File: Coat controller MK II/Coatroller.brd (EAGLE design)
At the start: 100 x 80 mm, 3 parts, among them U1 ATMEGA328P_PDIP, U2 V_REG_LDOSMD, Y1 ABM3B-16.000MHZ-B2-T

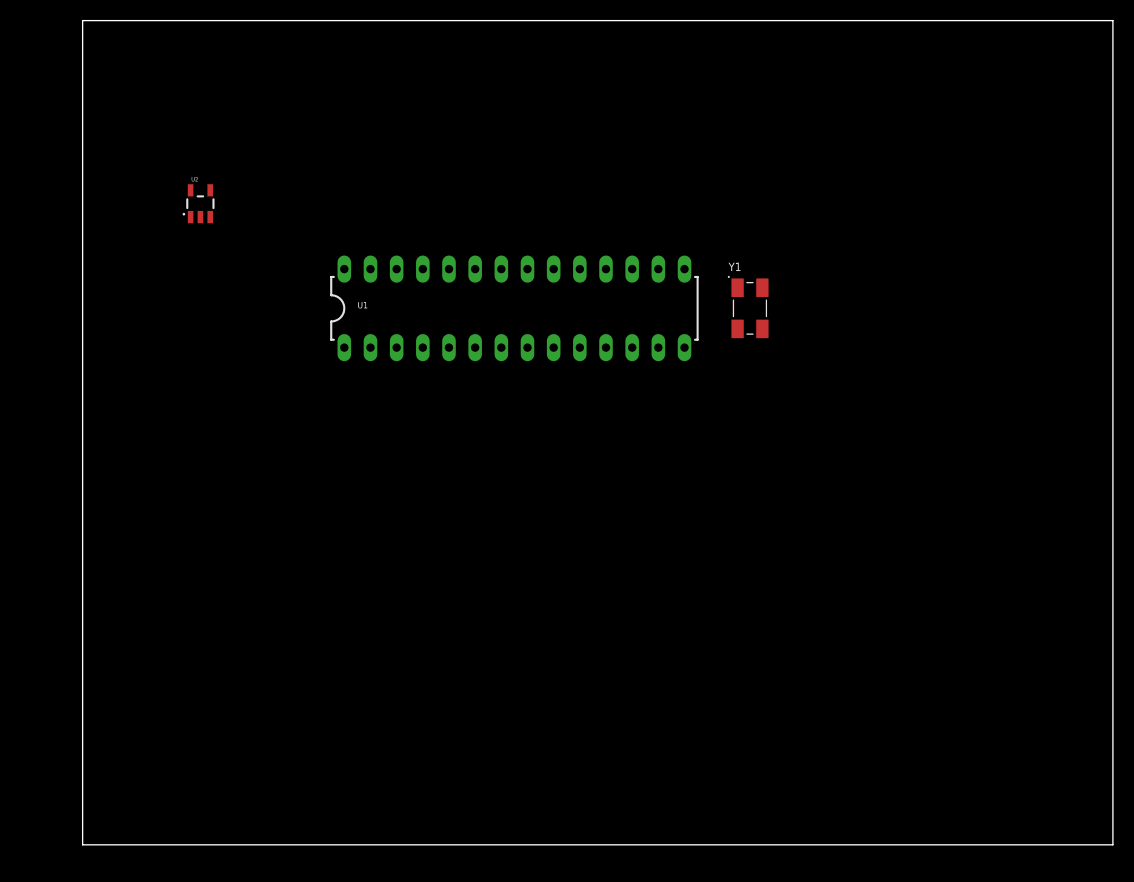
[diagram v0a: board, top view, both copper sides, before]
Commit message: added more parts
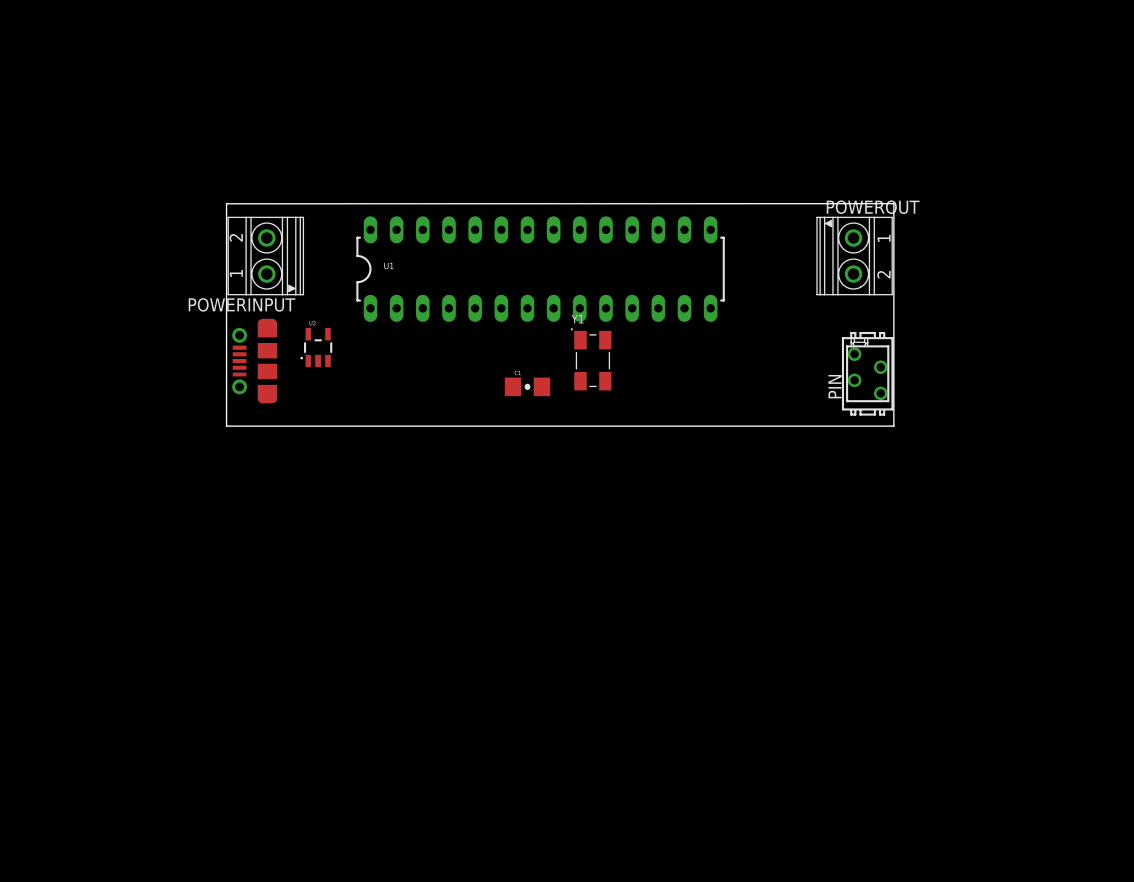
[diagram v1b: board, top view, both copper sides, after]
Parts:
- added C1: (no value), SparkFun-Capacitors:1206-CAP
- added PIN: MICROMATCH-4, con-amp-micromatch:MICROMATCH-4
- added POWERINPUT, POWEROUT: 1751248, con-phoenix-350:1751248
- added U$1: USB-CON-5PIN-105017-0001, GeekAmmo:USB-MICRO-MOLEX-105017-0001
- moved U2 18.1 mm to (22.9, 48.3)
- moved Y1 16.1 mm to (49.5, 47.0)
- moved U1 4.58 mm to (44.5, 55.9)
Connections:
- new net 5V: U1.7, U2.5
- new net GROUND: C1.2, PIN.4, POWERINPUT.1, POWEROUT.2, U$1.5, U1.8, U2.2
- new net N$1: U1.9, Y1.1
- new net N$2: U1.10, Y1.3
- new net N$3: C1.1, Y1.2, Y1.4
- new net N$4: PIN.3, U1.13
- new net N$5: PIN.2, U1.4
- new net VCC: PIN.1, POWERINPUT.2, POWEROUT.1, U$1.1, U2.1, U2.3
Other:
- board size 100 x 80 mm -> 64.8 x 21.6 mm
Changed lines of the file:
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@@
 <board>
 <plain>
-<wire x1="0" y1="0" x2="100" y2="0" width="0" layer="20"/>
-<wire x1="100" y1="0" x2="100" y2="80" width="0" layer="20"/>
-<wire x1="100" y1="80" x2="0" y2="80" width="0" layer="20"/>
-<wire x1="0" y1="80" x2="0" y2="0" width="0" layer="20"/>
+<wire x1="13.97" y1="40.64" x2="78.74" y2="40.64" width="0" layer="20"/>
+<wire x1="78.74" y1="40.64" x2="78.74" y2="62.23" width="0" layer="20"/>
+<wire x1="78.74" y1="62.23" x2="13.97" y2="62.22" width="0" layer="20"/>
+<wire x1="13.97" y1="62.22" x2="13.97" y2="40.64" width="0" layer="20"/>
 </plain>
 <attributes>
@@
 </autorouter>
 <elements>
-<element name="U1" library="SparkFun-DigitalIC" package="DIL28-3" value="ATMEGA328P_PDIP" x="41.91" y="52.07"/>
-<element name="U2" library="SparkFun-PowerIC" package="SOT23-5" value="V_REG_LDOSMD" x="11.43" y="62.23"/>
-<element name="Y1" library="ABM3B-16.000MHZ-B2-T" package="OSCSC500X320X110-4N" value="ABM3B-16.000MHZ-B2-T" x="64.77" y="52.07">
-<attribute name="PRICE" value="0.52 USD" x="64.77" y="52.07" size="1.778" layer="27" display="off"/>
-<attribute name="MP" value="ABM3B-16.000MHZ-B2-T" x="64.77" y="52.07" size="1.778" layer="27" display="off"/>
-<attribute name="PACKAGE" value="5.0 x 3.2mm Abracon" x="64.77" y="52.07" size="1.778" layer="27" display="off"/>
-<attribute name="DESCRIPTION" value="Crystal 16MHz %3F%3F20ppm %28Tol%29 %3F%3F50ppm %28Stability%29 18pF FUND 50Ohm 4-Pin CSMD T/R" x="64.77" y="52.07" size="1.778" layer="27" display="off"/>
-<attribute name="MF" value="Abracon" x="64.77" y="52.07" size="1.778" layer="27" display="off"/>
-<attribute name="AVAILABILITY" value="Good" x="64.77" y="52.07" size="1.778" layer="27" display="off"/>
+<element name="U1" library="SparkFun-DigitalIC" package="DIL28-3" value="ATMEGA328P_PDIP" x="44.45" y="55.88"/>
+<element name="U2" library="SparkFun-PowerIC" package="SOT23-5" value="V_REG_LDOSMD" x="22.86" y="48.26"/>
+<element name="Y1" library="ABM3B-16.000MHZ-B2-T" package="OSCSC500X320X110-4N" value="ABM3B-16.000MHZ-B2-T" x="49.53" y="46.99">
+<attribute name="PRICE" value="0.52 USD" x="49.53" y="46.99" size="1.778" layer="27" display="off"/>
+<attribute name="MP" value="ABM3B-16.000MHZ-B2-T" x="49.53" y="46.99" size="1.778" layer="27" display="off"/>
+<attribute name="PACKAGE" value="5.0 x 3.2mm Abracon" x="49.53" y="46.99" size="1.778" layer="27" display="off"/>
+<attribute name="DESCRIPTION" value="Crystal 16MHz %3F%3F20ppm %28Tol%29 %3F%3F50ppm %28Stability%29 18pF FUND 50Ohm 4-Pin CSMD T/R" x="49.53" y="46.99" size="1.778" layer="27" display="off"/>
+<attribute name="MF" value="Abracon" x="49.53" y="46.99" size="1.778" layer="27" display="off"/>
+<attribute name="AVAILABILITY" value="Good" x="49.53" y="46.99" size="1.778" layer="27" display="off"/>
+</element>
+<element name="POWERINPUT" library="con-phoenix-350" package="1751248" value="1751248" x="17.78" y="57.15" rot="R90">
+<attribute name="MF" value="" x="17.78" y="57.15" size="1.778" layer="27" font="vector" ratio="15" rot="R90" display="off"/>
+<attribute name="OC_NEWARK" value="unknown" x="17.78" y="57.15" size="1.778" layer="27" font="vector" ratio="15" rot="R90" display="off"/>
+<attribute name="OC_FARNELL" value="unknown" x="17.78" y="57.15" size="1.778" layer="27" font="vector" ratio="15" rot="R90" display="off"/>
+<attribute name="MPN" value="" x="17.78" y="57.15" size="1.778" layer="27" font="vector" ratio="15" rot="R90" display="off"/>
+</element>
+<element name="U$1" library="GeekAmmo" package="USB-MICRO-MOLEX-105017-0001" value="USB-CON-5PIN-105017-0001" x="15.24" y="44.45" rot="R90"/>
+<element name="POWEROUT" library="con-phoenix-350" package="1751248" value="1751248" x="74.93" y="57.15" rot="R270">
+<attribute name="MF" value="" x="74.93" y="57.15" size="1.778" layer="27" font="vector" ratio="15" rot="R270" display="off"/>
+<attribute name="OC_NEWARK" value="unknown" x="74.93" y="57.15" size="1.778" layer="27" font="vector" ratio="15" rot="R270" display="off"/>
+<attribute name="OC_FARNELL" value="unknown" x="74.93" y="57.15" size="1.778" layer="27" font="vector" ratio="15" rot="R270" display="off"/>
+<attribute name="MPN" value="" x="74.93" y="57.15" size="1.778" layer="27" font="vector" ratio="15" rot="R270" display="off"/>
+</element>
+<element name="C1" library="SparkFun-Capacitors" package="1206-CAP" value="" x="43.18" y="44.45"/>
+<element name="PIN" library="con-amp-micromatch" package="MICROMATCH-4" value="MICROMATCH-4" x="76.2" y="45.72" rot="R90">
+<attribute name="MF" value="" x="76.2" y="45.72" size="1.778" layer="27" font="vector" ratio="15" rot="R90" display="off"/>
+<attribute name="OC_NEWARK" value="19R8124" x="76.2" y="45.72" size="1.778" layer="27" font="vector" ratio="15" rot="R90" display="off"/>
+<attribute name="OC_FARNELL" value="3784629" x="76.2" y="45.72" size="1.778" layer="27" font="vector" ratio="15" rot="R90" display="off"/>
+<attribute name="MPN" value="7-215464-4" x="76.2" y="45.72" size="1.778" layer="27" font="vector" ratio="15" rot="R90" display="off"/>
 </element>
 </elements>
 <signals>
+<signal name="GROUND">
+<contactref element="POWERINPUT" pad="1"/>
+<contactref element="POWEROUT" pad="2"/>
+<contactref element="U2" pad="2"/>
+<contactref element="U$1" pad="5"/>
+<contactref element="U1" pad="8"/>
+<contactref element="C1" pad="2"/>
+<contactref element="PIN" pad="4"/>
+<wire x1="45.72" y1="52.07" x2="74.83" y2="55.4" width="0" layer="19" extent="1-1"/>
+<wire x1="44.58" y1="44.45" x2="45.72" y2="52.07" width="0" layer="19" extent="1-1"/>
+<wire x1="22.86" y1="46.9599" x2="44.58" y2="44.45" width="0" layer="19" extent="1-1"/>
+<wire x1="15.24" y1="48.25" x2="22.86" y2="46.9599" width="0" layer="19" extent="1-1"/>
+<wire x1="17.88" y1="55.4" x2="22.86" y2="46.9599" width="0" layer="19" extent="1-1"/>
+<wire x1="77.47" y1="43.815" x2="44.58" y2="44.45" width="0" layer="19" extent="1-1"/>
+</signal>
+<signal name="VCC">
+<contactref element="POWERINPUT" pad="2"/>
+<contactref element="U$1" pad="1"/>
+<contactref element="U2" pad="3"/>
+<contactref element="POWEROUT" pad="1"/>
+<contactref element="U2" pad="1"/>
+<contactref element="PIN" pad="1"/>
+<wire x1="74.93" y1="47.625" x2="74.83" y2="58.9" width="0" layer="19" extent="1-1"/>
+<wire x1="23.81" y1="46.9599" x2="74.93" y2="47.625" width="0" layer="19" extent="1-1"/>
+<wire x1="21.91" y1="46.9599" x2="23.81" y2="46.9599" width="0" layer="19" extent="1-1"/>
+<wire x1="15.24" y1="45.65" x2="21.91" y2="46.9599" width="0" layer="19" extent="1-1"/>
+<wire x1="17.88" y1="58.9" x2="21.91" y2="46.9599" width="0" layer="19" extent="1-1"/>
+</signal>
+<signal name="5V">
+<contactref element="U2" pad="5"/>
+<contactref element="U1" pad="7"/>
+<wire x1="21.91" y1="49.5601" x2="43.18" y2="52.07" width="0" layer="19" extent="1-1"/>
+</signal>
+<signal name="N$1">
+<contactref element="Y1" pad="1"/>
+<contactref element="U1" pad="9"/>
+<wire x1="48.33" y1="48.99" x2="48.26" y2="52.07" width="0" layer="19" extent="1-1"/>
+</signal>
+<signal name="N$2">
+<contactref element="Y1" pad="3"/>
+<contactref element="U1" pad="10"/>
+<wire x1="50.73" y1="44.99" x2="50.8" y2="52.07" width="0" layer="19" extent="1-1"/>
+</signal>
+<signal name="N$3">
+<contactref element="Y1" pad="4"/>
+<contactref element="Y1" pad="2"/>
+<contactref element="C1" pad="1"/>
+<wire x1="48.33" y1="44.99" x2="50.73" y2="48.99" width="0" layer="19" extent="1-1"/>
+<wire x1="41.78" y1="44.45" x2="48.33" y2="44.99" width="0" layer="19" extent="1-1"/>
+</signal>
+<signal name="N$5">
+<contactref element="PIN" pad="2"/>
+<contactref element="U1" pad="4"/>
+<wire x1="77.47" y1="46.355" x2="35.56" y2="52.07" width="0" layer="19" extent="1-1"/>
+</signal>
+<signal name="N$4">
+<contactref element="PIN" pad="3"/>
+<contactref element="U1" pad="13"/>
+<wire x1="74.93" y1="45.085" x2="58.42" y2="52.07" width="0" layer="19" extent="1-1"/>
+</signal>
 </signals>
 </board>

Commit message: finished placing and routing
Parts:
- moved POWEROUT 46.0 mm to (53.3, 16.5)
- moved PIN 44.4 mm to (53.3, 7.62)
- moved POWERINPUT 43.0 mm to (3.81, 16.5)
- moved U1 43.0 mm to (30.5, 15.2)
- moved Y1 43.0 mm to (35.6, 6.35), turned to 270 degrees
- moved U$1 41.7 mm to (0.76, 5.33)
- moved C1 41.5 mm to (28.3, 5.71), turned to 90 degrees
- moved U2 40.6 mm to (8.89, 10.2), turned to 270 degrees
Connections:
- removed net N$4: PIN.3, U1.13
- removed net N$5: PIN.2, U1.4
- new net CLOCK: PIN.3, U1.6
- new net DATA: PIN.2, U1.13
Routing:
- net VCC: track 0.00 -> 34.0 mm
- net CLOCK: track 0.00 -> 27.2 mm
- net 5V: track 0.00 -> 22.0 mm
- net N$2: track 0.00 -> 17.9 mm
- net GROUND: track 0.00 -> 15.2 mm
- net N$3: track 0.00 -> 11.6 mm
- net DATA: track 0.00 -> 11.5 mm
- net N$1: track 0.00 -> 5.72 mm
- added copper zone on layer 1, net GROUND
- added copper zone on layer 16, net VCC
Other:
- board size 64.8 x 21.6 mm -> 58.4 x 21.6 mm
- board text added: "+"
- board text added: "-"
- board text added: "5v"
- board text added: "ABM3B"
- board text added: "C1"
- board text added: "Clock"
- board text added: "Data"
- board text added: "Ground"
- board text added: "Input"
- board text added: "Made by Remington Winters"
- board text added: "Output"
- board text added: "RGB Coat Controller Mk II 2017 - Burning Man Made for Marrie - Cause she's so foxy"
- board text added: "v_reg_5v"
